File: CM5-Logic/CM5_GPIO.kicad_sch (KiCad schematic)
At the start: 17 parts, among them J13 JST_SHBM04B-SRSS-TB, J14 Micro_SD_Card_Det, U5 74LVC1G07SE-7, U6 TPD4EUSB30, U7 TPD4EUSB30, U8 RT9742GGJ5, U9 MagJack-A70-112-331N126

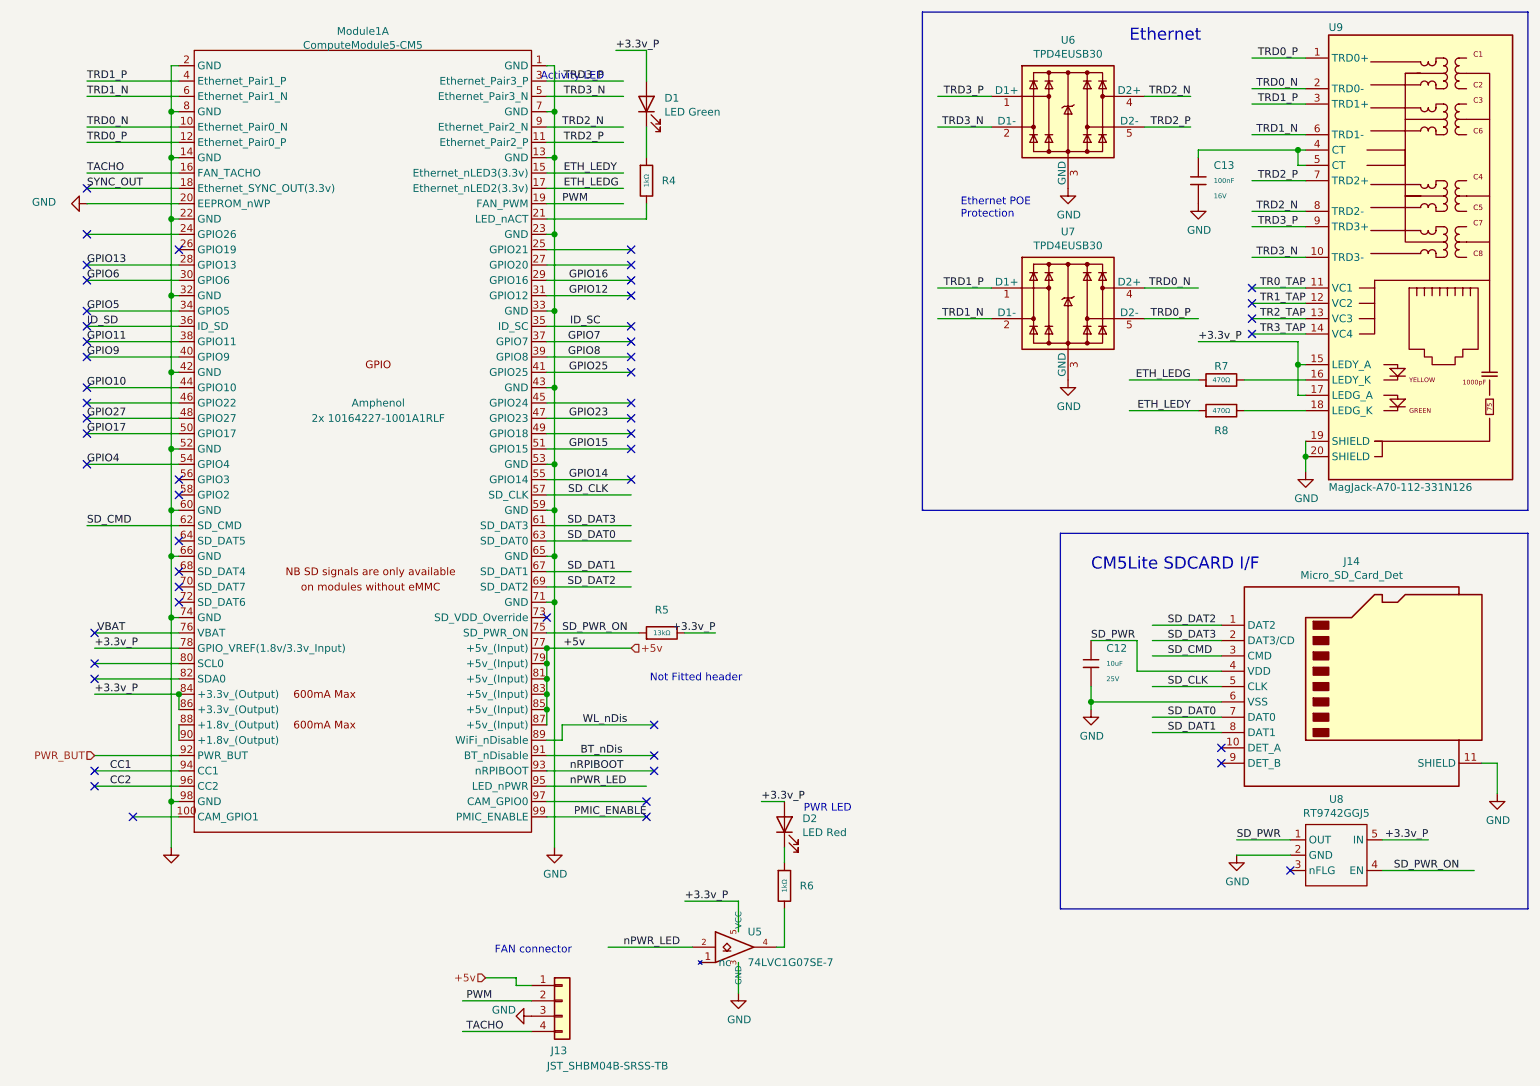
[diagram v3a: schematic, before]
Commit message: changes USB port, adds TMC2209 SilentStepStick footprint, redoes PCB Layout
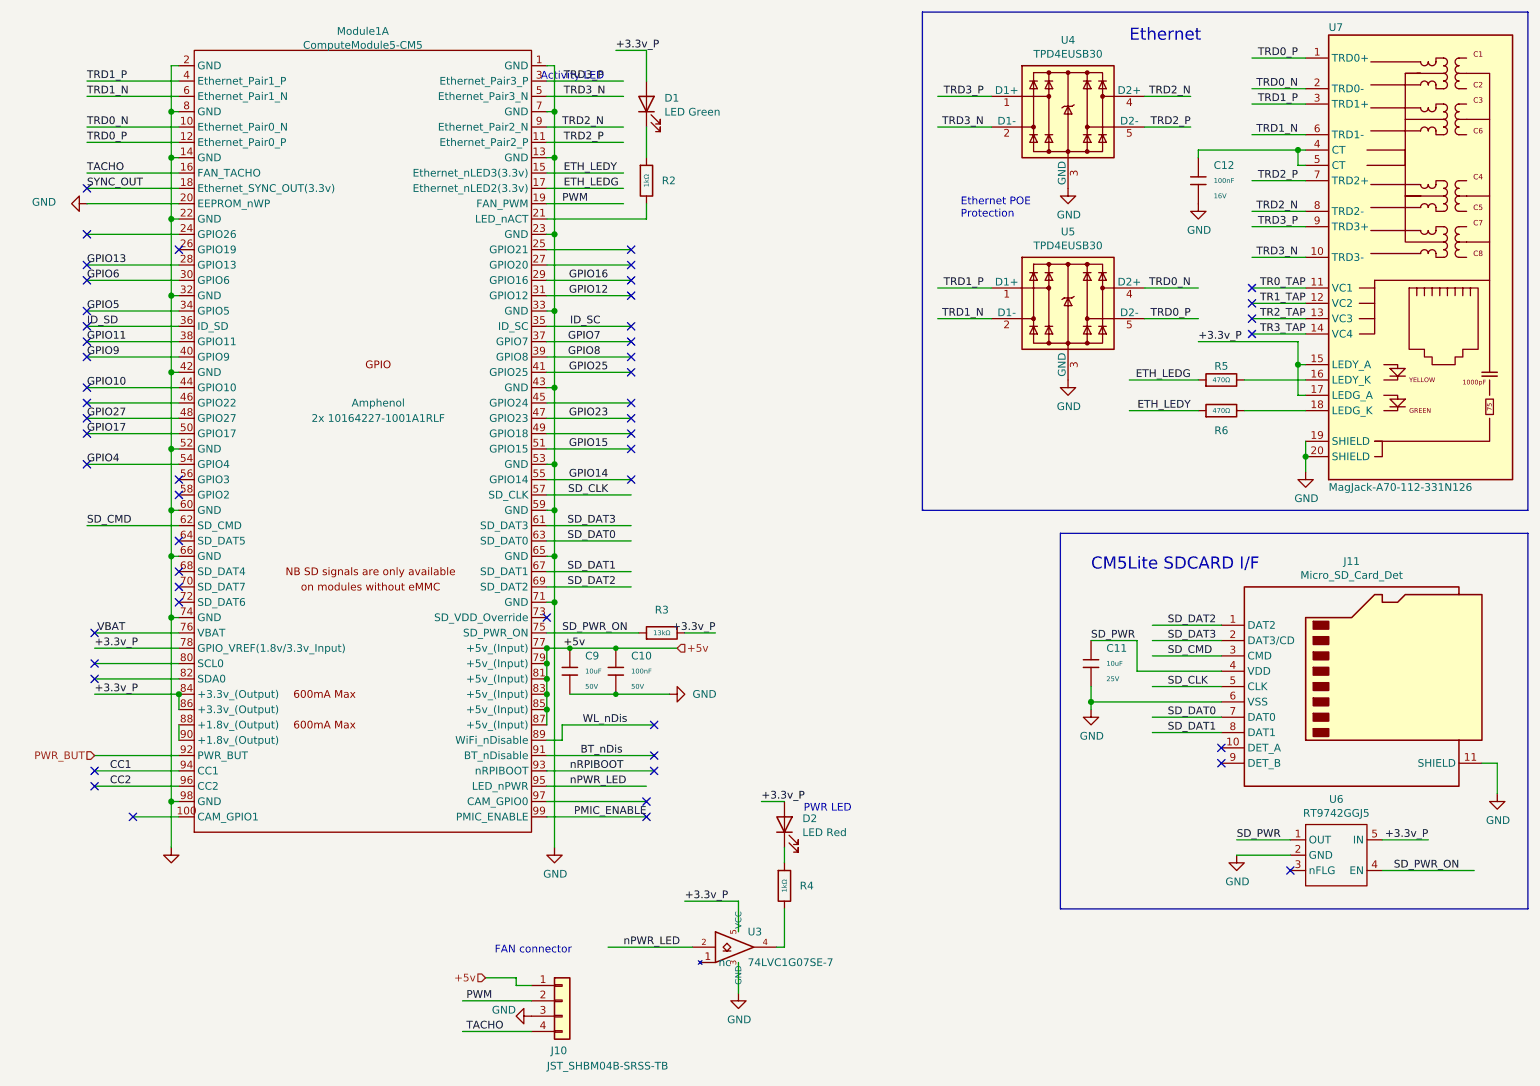
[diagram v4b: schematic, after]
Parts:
- added C10: 100nF, PCM_JLCPCB:C_0603, symbol PCM_JLCPCB-Capacitors:0603,100nF
- added C9: 10uF, PCM_JLCPCB:C_1206, symbol PCM_JLCPCB-Capacitors:1206,10uF
- renumbered C12 to C11, C13 to C12, J13 to J10, J14 to J11, R4 to R2, R5 to R3, R6 to R4, R7 to R5, R8 to R6, U5 to U3, U6 to U4, U7 to U5, U8 to U6, U9 to U7
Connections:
- net +5v: now also C10.1, C9.1
- net GND: now also C10.2, C9.2
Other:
- note removed: "Not Fitted header"

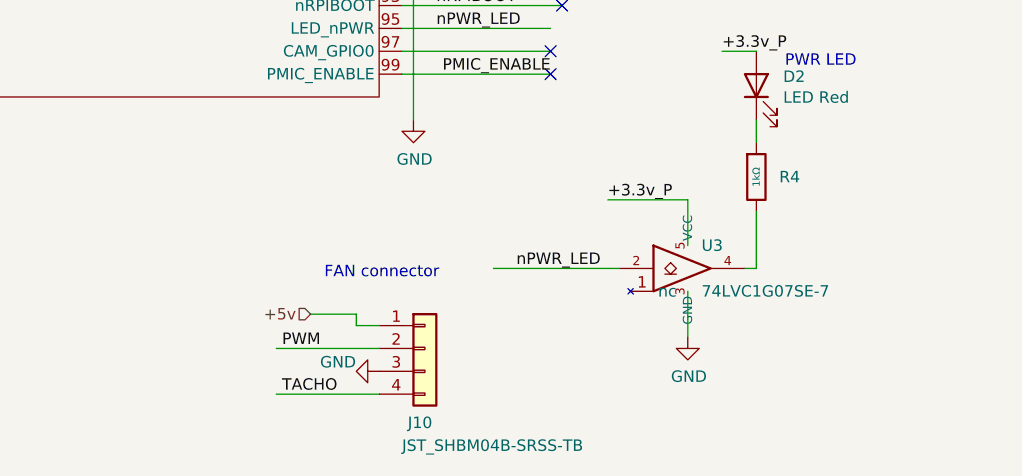
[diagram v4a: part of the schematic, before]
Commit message: Finishes PCB Pad Layout, Updates LED Status Circuit to RPI Foundations newest version
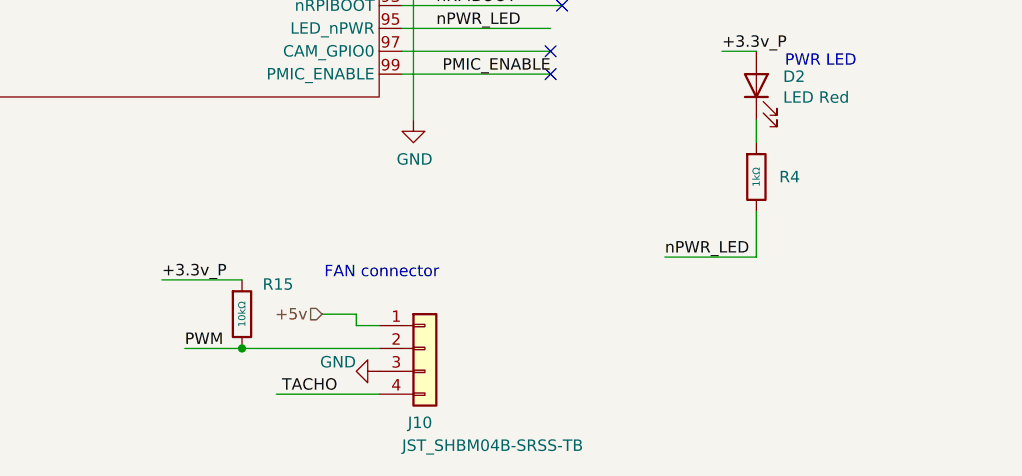
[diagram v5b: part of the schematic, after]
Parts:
- removed U3: 74LVC1G07SE-7, Package_TO_SOT_SMD:SOT-353_SC-70-5, symbol CM5IO:74LVC1G07_copy
- added R15: 10kΩ, PCM_JLCPCB:R_0402, symbol PCM_JLCPCB-Resistors:0402,10kΩ
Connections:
- net +3.3v_P: now also R15.1
- net PWM: now also R15.2
- net nPWR_LED: now also R4.2
